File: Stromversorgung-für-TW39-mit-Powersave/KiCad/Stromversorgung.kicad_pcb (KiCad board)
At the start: 2 copper layers, 81.3 x 104.1 mm, 19 parts, among them J1 230V~ IN, J2 RP, J3 +5V, J4 230V~ OUT, J5 +90V, K1 FINDER-40.52, Q1 BC337, T1 GERTH 422.60.2

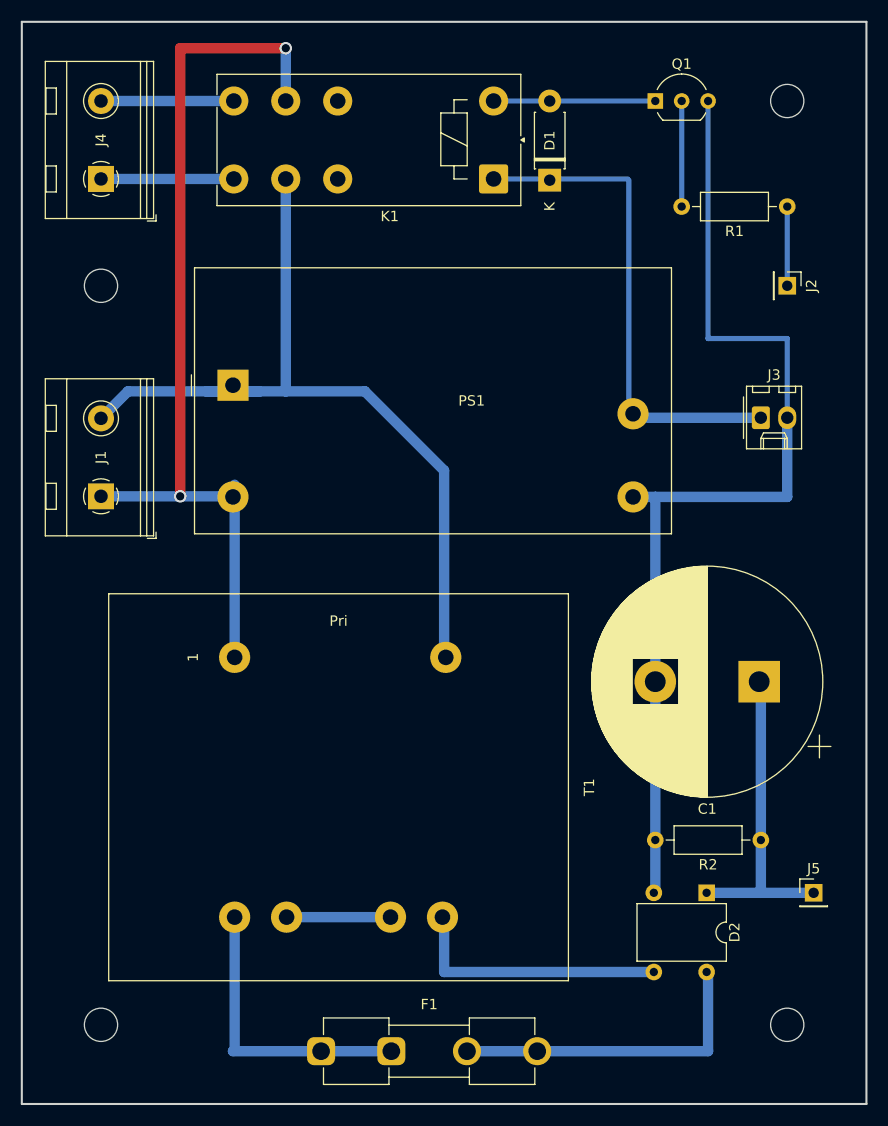
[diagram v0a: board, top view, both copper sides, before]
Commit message: bugfix in KiCad
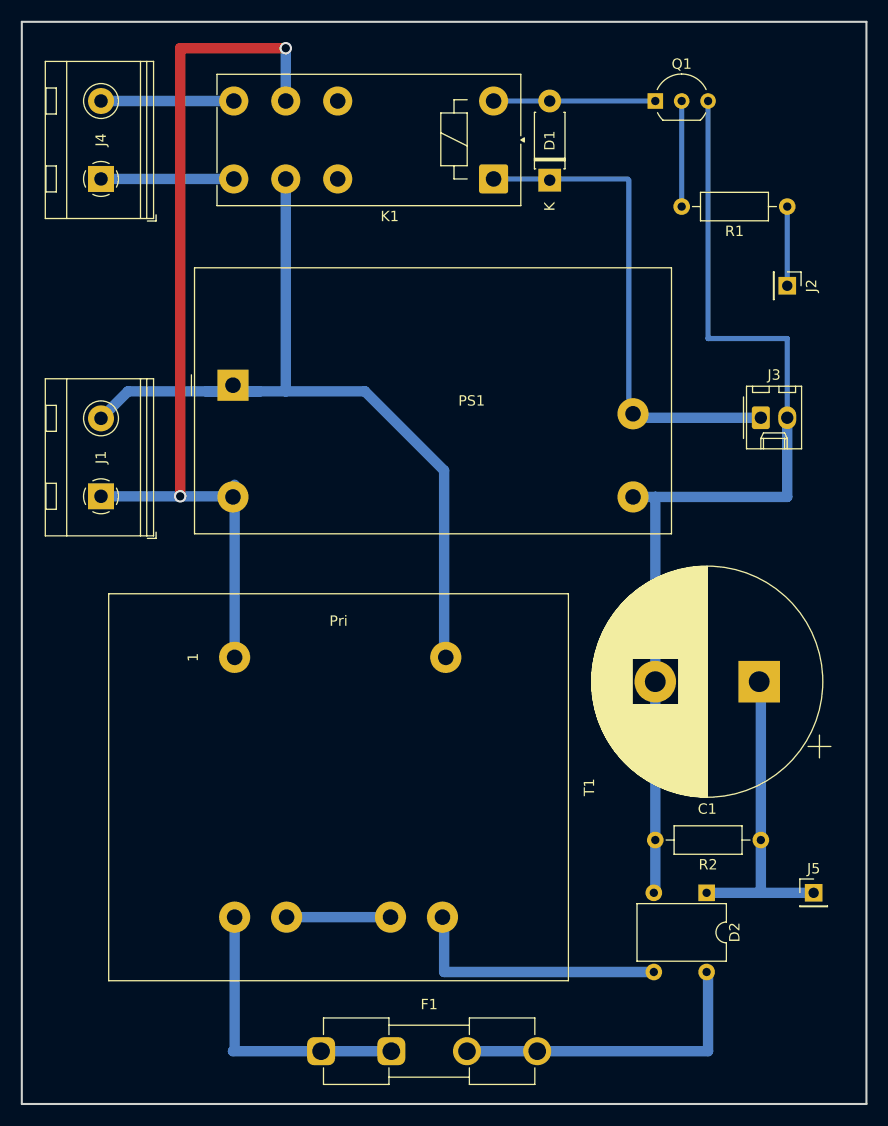
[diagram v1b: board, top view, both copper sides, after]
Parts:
- removed REF** (x4): MountingHole_3.2mm_M3, MountingHole:MountingHole_3.2mm_M3
- F1: value 80mAT -> 100mAT
- T1: value GERTH 422.60.2 -> GERTH 421.48.2
